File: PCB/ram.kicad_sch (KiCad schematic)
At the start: 31 parts, among them SW5 SW_DIP_x08, SW6 SW_Push, U20 74LS157, U21 74189, U22 74LS157, U23 74189, U24 74LS157, U25 74LS245, U26 74LS00, U27 74LS04, U28 74LS04

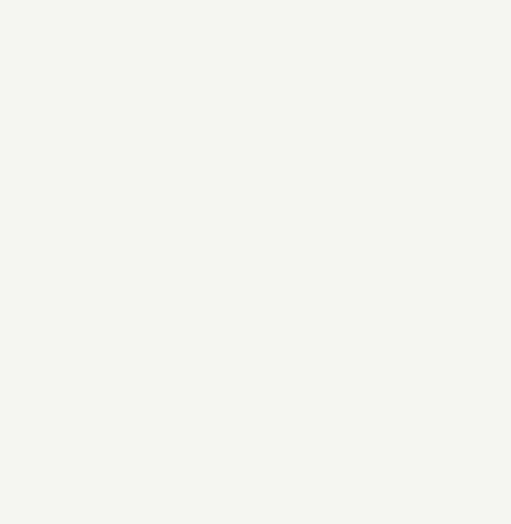
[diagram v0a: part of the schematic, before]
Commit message: Cleaned up the schematic and got started on assigning all the footprints to the symbols
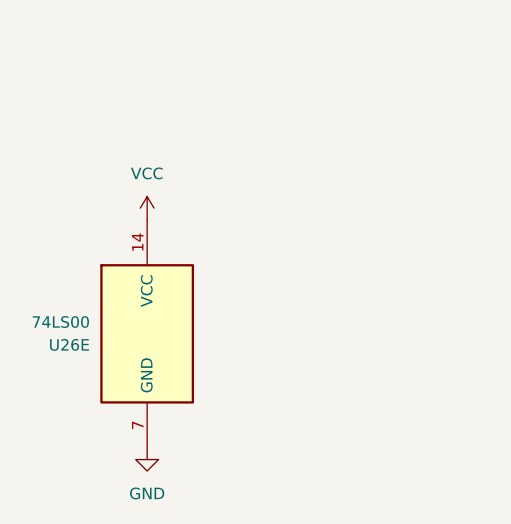
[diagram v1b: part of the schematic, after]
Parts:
- added unit 1 of U26
- C12, C13, C14: footprint (none) -> Capacitor_THT:C_Radial_D5.0mm_H5.0mm_P2.00mm
- D26, D27, D28, D29, D30, D31, D32, D33: footprint (none) -> LED_THT:LED_D1.8mm_W1.8mm_H2.4mm_Horizontal_O1.27mm_Z1.6mm
- R24, R25, R26, R27, R28, R29, R30, R31, R32: footprint (none) -> Resistor_THT:R_Axial_DIN0207_L6.3mm_D2.5mm_P7.62mm_Horizontal
- SW5: footprint (none) -> Button_Switch_THT:SW_DIP_SPSTx08_Slide_6.7x21.88mm_W7.62mm_P2.54mm_LowProfile
- SW6: footprint (none) -> Button_Switch_THT:SW_PUSH_6mm
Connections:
- net GND: now also U26.7 (GND)
- net RI: now also U26.2; no longer U26.2
- net VCC: now also U26.14 (VCC)
- net at C14.2, R32.1: now also U26.1; no longer U26.1
- net at U20.10 (I1c): now also U26.3; no longer U26.3

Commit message: added more models to work with on my pcb
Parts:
- removed U20, U22, U24: 74LS157, symbol 74xx:74LS157
- added U20, U22, U5: 74LS04, Package_DIP:DIP-14_W7.62mm, symbol 74xx:74LS04
- added U24, U51, U52: 74LS158, Package_DIP:DIP-16_W7.62mm, symbol 74xx:74LS158
- D26, D27, D28, D29, D30, D31, D32, D33: value LED -> RED; footprint LED_THT:LED_D1.8mm_W1.8mm_H2.4mm_Horizontal_O1.27mm_Z1.6mm -> LED_THT:LED_D3.0mm
- U21, U23: footprint (none) -> Custom:N16
- U25: footprint (none) -> Custom:DIP254P762X508-20
- U26, U27, U28: footprint (none) -> Custom:N14
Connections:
- net BUS_0: now also U24.10 (I1d)
- net BUS_1: now also U24.13 (I1c)
- net BUS_2: now also U24.6 (I1b)
- net BUS_3: now also U24.3 (I1a)
- net GND: now also U28.7 (GND), U20.7 (GND), U22.7 (GND), U24.1 (S), U24.15 (E), U24.8 (GND), U51.1 (S), U51.15 (E), U51.8 (GND), U52.1 (S), U52.10 (I1d), U52.11 (I0d), U52.13 (I1c), U52.14 (I0c), U52.15 (E), U52.2 (I0a), U52.3 (I1a), U52.5 (I0b), U52.6 (I1b), U52.8 (GND)
- net VCC: now also U28.14 (VCC), U20.14 (VCC), U22.14 (VCC), U24.16 (VCC), U51.16 (VCC), U52.16 (VCC)
- net at U21.10 (D2): now also U20.12
- net at U21.12 (D3): now also U5.10
- net at U21.3 (~{WE}), U23.3 (~{WE}), U27.11: now also U20.2
- net at U21.4 (D0): now also U23.6 (D1), U20.4, U5.6
- net at U21.5 (~{O}0), U23.12 (D3): now also U22.2
- net at U21.6 (D1): now also U20.6
- net at U23.10 (D2): now also U5.4
- net at U23.4 (D0): now also U20.8, U52.9 (Zd)
- net at SW5.1: now also U24.11 (I0d)
- net at SW5.13: now also U24.2 (I0a)
- net at SW5.14: now also U24.5 (I0b)
- net at SW5.2: now also U24.14 (I0c)
- net at SW6.2: now also U51.14 (I0c)
- net at U26.3: now also U51.13 (I1c)
- new net: U20.1, U51.12 (Zc)
- new net: U5.5, U52.12 (Zc)
- new net: U22.1, U52.4 (Za)
- new net: U5.3, U52.7 (Zb)
- new net: U20.3, U24.9 (Zd)
- new net: U20.5, U24.12 (Zc)
- new net: U24.4 (Za), U5.11
- new net: U20.13, U24.7 (Zb)

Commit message: got the PCB layed out into one group and started routing the traces and fixing DRC errors.
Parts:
- added unit 7 of U20
- added unit 3 of U20
- added unit 2 of U20
- added unit 2 of U28
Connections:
- net GND: now also U20.7 (GND); no longer U20.7 (GND)
- net VCC: now also U20.14 (VCC); no longer U20.14 (VCC)
- net at U21.4 (D0), U23.6 (D1), U5.6: now also U20.4; no longer U20.4
- net at U21.11 (~{O}3): now also U28.3; no longer U28.3
- net at U21.6 (D1): now also U20.6; no longer U20.6
- net at D33.2 (A), U25.9 (A7): now also U28.4; no longer U28.4
- net at U24.9 (Zd): now also U20.3; no longer U20.3
- net at U24.12 (Zc): now also U20.5; no longer U20.5
